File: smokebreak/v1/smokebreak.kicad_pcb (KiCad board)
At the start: 4 copper layers, 94 x 52 mm, 186 parts, among them J1 XT60 male, J2 XT30 male, J3 XT60 female, J4 XT30 female, J5 JST-XH 9, J6 SWD, J7 TFT1901 FPC, J8 USB-C, Q1 input FET, Q10 BC817, Q2 output FET, Q3 DMP10H400SE, Q4 BC817, Q5 BC817, Q6 AO3401A, Q7 AO3401A, Q8 2N7002, Q9 AO3400A, SW1 ON-OFF-(ON), SW2 Limit -, SW3 Limit +, U1 TPS48000, U10 SN74AHCT1G125, U11 USBLC6-2SC6, U2 INA181A2, U3 LMR36506R5, U4 TLV75533, U5 STM32G0B1RBT6, U6 DRV5032FA, U7 74LVC1G11, U8 LMV331, U9 SN74LVC1G74

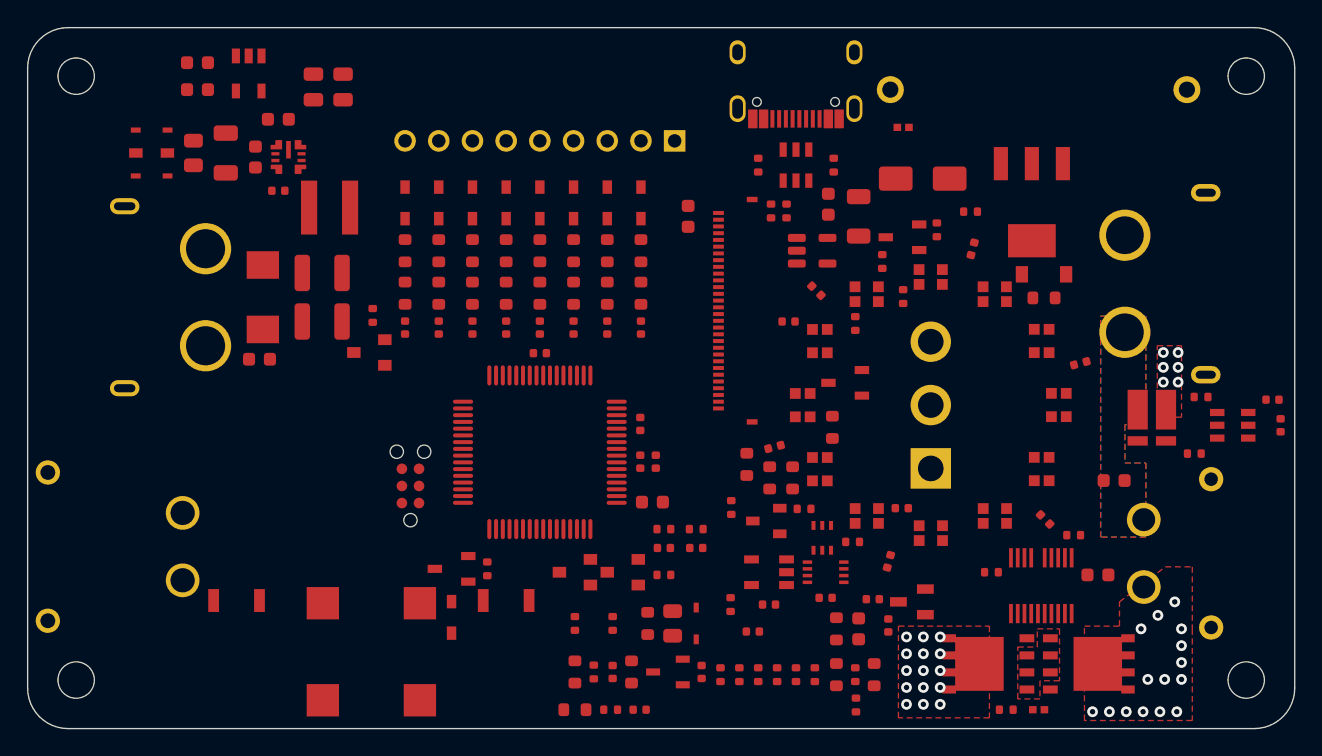
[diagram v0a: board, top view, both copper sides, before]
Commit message: smokebreak v1: simulation design values in the circuit (damper, snubber, Cdvdt, gate clamp, hard-short comparator, 2 x 15 Ohm pre-charge, DPAK pre-charge FET, 150 V probe PNPs), re-placed north-east, mesh 3D models
Co-Authored-By: Claude Opus 5.5 <noreply@anthropic.com>
Claude-Session: https://claude.ai/code/session_01SBnFJLvm1wBa1jZy4RXnma
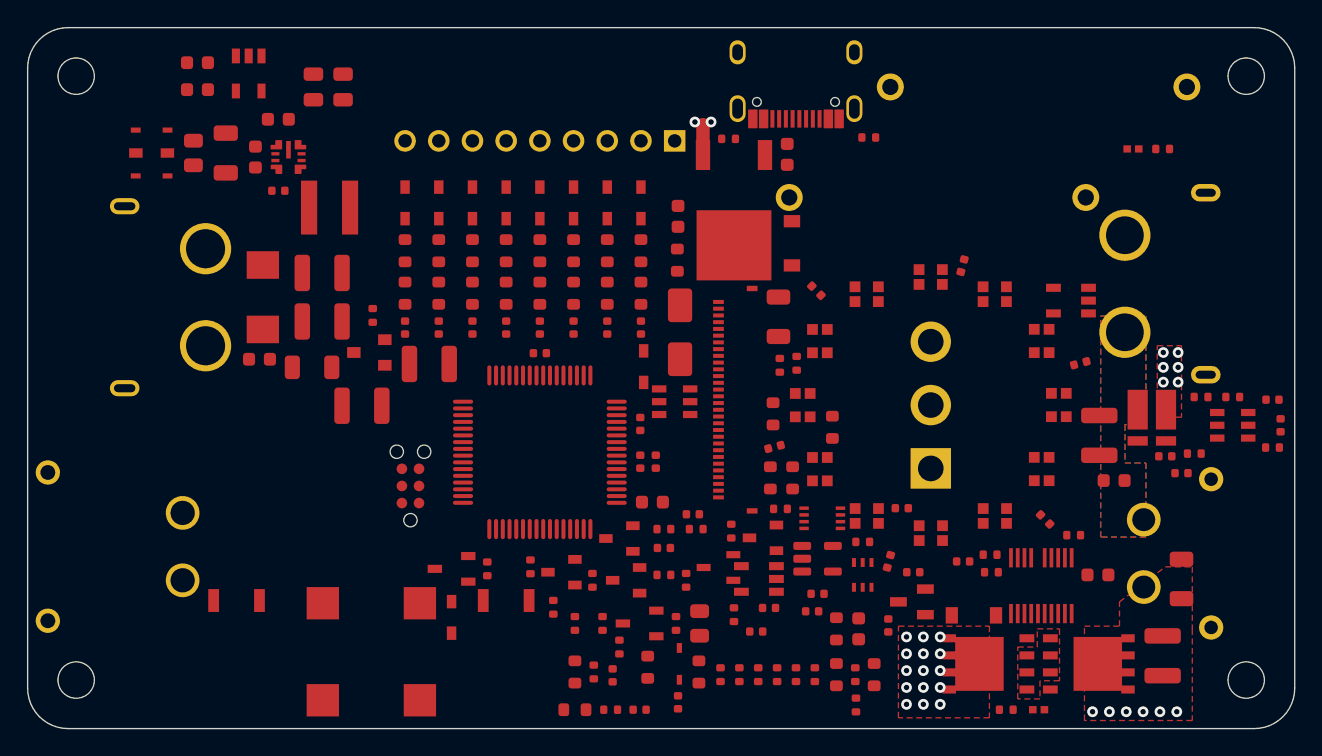
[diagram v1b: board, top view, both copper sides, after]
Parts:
- added C50: 4u7F 100V, C_1210_3225Metric, F.Cu at (129.8, 125.0)
- added C51: 4u7F 100V, C_1210_3225Metric, F.Cu at (124.8, 128.1)
- added C52: 4u7F 100V, C_1210_3225Metric, F.Cu at (184.2, 146.6)
- added C53: 4u7F 100V, C_1210_3225Metric, F.Cu at (179.5, 130.2)
- added C54: 22nF 50V, C_0402_1005Metric, F.Cu at (169.4, 139.6)
- added C55: 100nF 16V, C_0402_1005Metric, F.Cu at (184.4, 131.8)
- added C56: 100nF 16V, C_0402_1005Metric, F.Cu at (185.6, 133.1)
- added D18: 15 V, SOD-123_L2.7-W1.6-LS3.7-RD, F.Cu at (170.2, 143.6)
- added D19: 1N4148WS, SOD-323_L1.8-W1.3-LS2.5-RD, F.Cu at (145.7, 125.2)
- added R67: 0.33 Ohm, R_1206_3216Metric, F.Cu at (121.1, 125.2)
- added R68: 0.47 Ohm, R_1206_3216Metric, F.Cu at (185.6, 140.9)
- added R69: 1 k, R_0402_1005Metric, F.Cu at (171.4, 139.1)
- added R70: 39 k, R_0402_1005Metric, F.Cu at (189.4, 127.4)
- added R71: 1 k, R_0402_1005Metric, F.Cu at (192.3, 131.2)
- added R72: 4.7 k, R_0402_1005Metric, F.Cu at (137.3, 140.0)
- added R73: 820 Ohm, R_0402_1005Metric, F.Cu at (139.0, 143.0)
- added R_PRE2: 15 Ohm 5 W, RES-TH_BD7.5-L18.0-P22.00-D1.0, F.Cu at (167.5, 112.6)
- added U12: LMV331, SOT-23-5_L3.0-W1.7-P0.95-LS2.8-BR, F.Cu at (177.4, 120.2)
- Q3: value DMP10H400SE -> SUD50P10-43L; footprint SOT-223_L6.5-W3.5-P2.30-LS7.0-BR -> TO-252-3_L6.5-W5.8-P4.58-BR
- Q4: value BC817 -> MMBTA42; footprint SOT-23-3_L2.9-W1.6-P1.90-LS2.8-BR -> SOT-23-3_L2.9-W1.3-P1.90-LS2.4-BR
- Q6, Q7: value AO3401A -> MMBT5401; footprint SOT-23_L2.9-W1.3-P1.90-LS2.4-BR -> SOT-23-3_L2.9-W1.3-P1.90-LS2.4-BR
- R6: value 47 Ohm -> 100 k
- R9: value 15.4 k -> 40.2 k
- R_PRE: value 22 Ohm 5 W -> 15 Ohm 5 W
- moved R23 36.5 mm to (141.9, 141.0)
- moved R24 32.9 mm to (142.7, 144.2)
- moved Q4 32.7 mm to (144.4, 141.0)
- moved R21 27.8 mm to (148.8, 141.0)
- moved R19 27.3 mm to (148.2, 117.2), turned to 90 degrees
- moved R22 25.9 mm to (148.1, 144.2)
- moved Q5 23.5 mm to (145.4, 144.2)
- moved U10 22.9 mm to (158.6, 139.4)
- moved Q3 22.1 mm to (152.4, 112.8)
- moved D3 21.3 mm to (148.4, 122.6), turned to 90 degrees
- moved C42 20.3 mm to (158.6, 142.0)
- moved U11 19.7 mm to (148.0, 127.8), turned to 90 degrees
- moved D2 18.8 mm to (156.7, 116.0), turned to 90 degrees
- moved LED1 18.4 mm to (162.2, 136.2), turned to 180 degrees
- moved LED10 18.4 mm to (175.2, 132.8), turned to -90 degrees
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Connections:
- Q6 pad 1: PROBE_1K_N -> PROBE_BB1
- Q7 pad 1: PROBE_100_N -> PROBE_BB2
- R20 pad 2: PRE_PULL -> PRE_R
- R26 pad 1: PROBE_1K_N -> PROBE_BB1
- R27 pad 1: PROBE_100_N -> PROBE_BB2
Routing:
- net VIN: track 0.00 -> 2.20 mm, vias 15 -> 17
- net VOUT: vias 15 -> 6

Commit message: smokebreak v1: reverse-battery FET Q11 in the battery return (sims pass 22/22 with small damper and snubber), balance black wire through 10 Ohm, placement DRC clean
Co-Authored-By: Claude Opus 5.5 <noreply@anthropic.com>
Claude-Session: https://claude.ai/code/session_01SBnFJLvm1wBa1jZy4RXnma
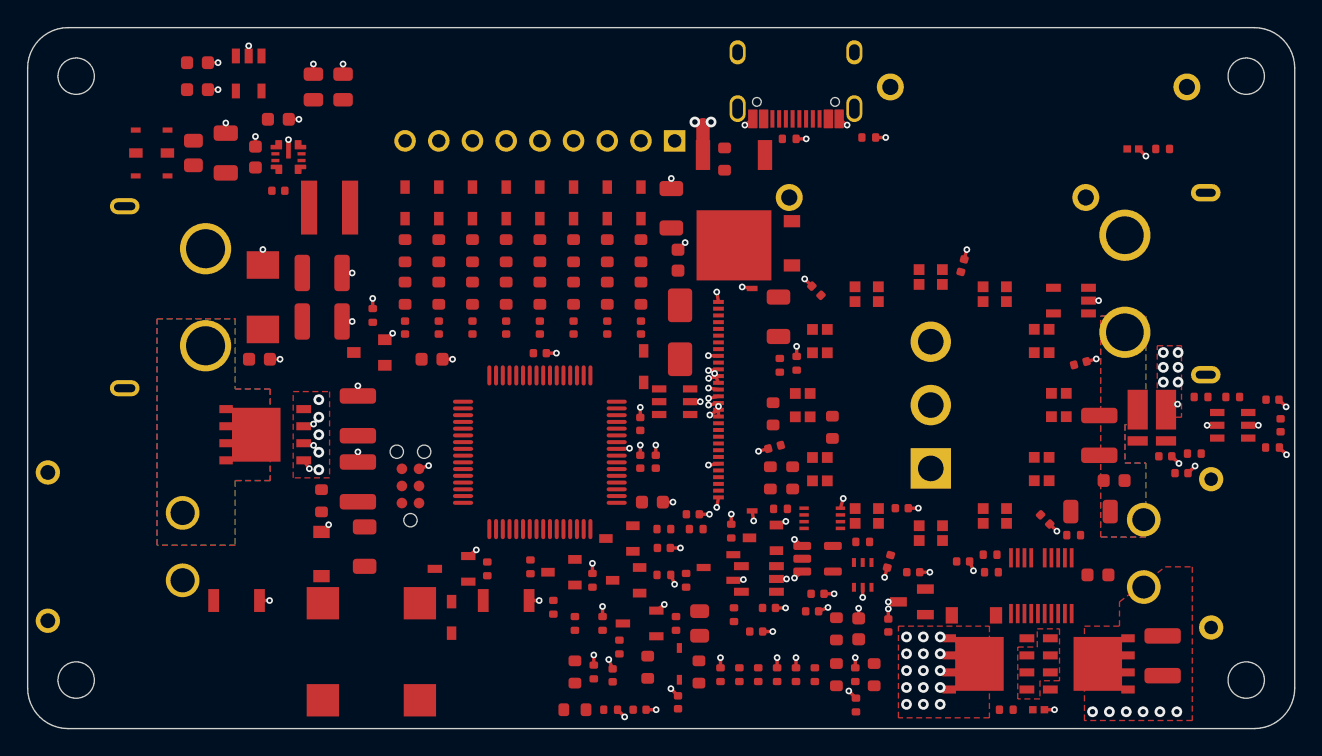
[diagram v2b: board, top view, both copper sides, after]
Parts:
- added D20: 12 V, SOD-123_L2.7-W1.6-LS3.7-RD, F.Cu at (121.8, 139.1)
- added Q11: BSC070N10LS5, PG-TDSON-8_L5.9-W5.1-P1.27-LS6.1-BL, F.Cu at (117.6, 130.2)
- added R74: 4.7 M, R_0603_1608Metric, F.Cu at (121.8, 135.1)
- added R75: 10 Ohm, R_1206_3216Metric, F.Cu at (147.8, 113.4)
- R70: value 39 k -> 49.9 k
- moved C49 30.4 mm to (130.0, 124.6), turned to 0 degrees
- moved R67 13.9 mm to (125.0, 138.5), turned to 90 degrees
- moved R68 8.40 mm to (178.8, 135.9), turned to 0 degrees
- moved R19 8.28 mm to (151.7, 109.8)
- moved C50 6.55 mm to (124.5, 128.8), turned to 90 degrees
- moved C51 5.66 mm to (124.5, 133.7), turned to 90 degrees
- moved R63 4.50 mm to (156.5, 108.2)
- moved C41 3.25 mm to (148.2, 117.2)
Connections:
- J1 pad 1: GND -> BATT_NEG
- J2 pad 1: GND -> BATT_NEG
- J5 pad 1: GND -> BAL1
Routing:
- net GND: track 0.00 -> 78.8 mm, vias 6 -> 115
- added copper zone on B.Cu, net BATT_NEG
- added copper zone on F.Cu, net BATT_NEG

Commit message: smokebreak v1: placed board with the TPS48000 move and ground fan-out
Co-Authored-By: Claude Opus 5.5 <noreply@anthropic.com>
Claude-Session: https://claude.ai/code/session_01SBnFJLvm1wBa1jZy4RXnma
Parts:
- moved C5 17.4 mm to (162.2, 142.5)
- moved U1 15.1 mm to (161.7, 148.1), turned to -90 degrees
- moved U12 10.9 mm to (179.4, 131.0)
- moved R32 10.8 mm to (139.1, 147.8)
- moved R5 9.55 mm to (168.2, 143.5)
- moved U9 9.39 mm to (150.4, 140.4)
- moved R4 6.75 mm to (156.1, 148.0)
- moved U7 6.50 mm to (168.4, 140.3)
- moved C53 6.50 mm to (179.5, 136.8)
- moved R7 6.03 mm to (176.6, 143.6)
- moved R6 5.85 mm to (165.7, 140.3)
- moved R68 5.75 mm to (178.8, 141.7)
- moved D5 4.81 mm to (147.0, 137.8)
- moved C12 4.70 mm to (169.9, 142.4)
- moved R69 4.67 mm to (169.8, 143.5)
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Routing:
- net GND: track 78.8 -> 78.5 mm, vias 115 -> 114

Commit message: smokebreak v1: 6-layer stack (F sig, In1 GND, In2/In3 sig, In4 VIN|VOUT power, B sig) - the 4-layer board could not route the control district
Co-Authored-By: Claude Opus 5.5 <noreply@anthropic.com>
Claude-Session: https://claude.ai/code/session_01SBnFJLvm1wBa1jZy4RXnma
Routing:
- added copper zone on In4.Cu, net VIN
- added copper zone on In4.Cu, net VOUT
- removed copper zone on In2.Cu, net VIN
- removed copper zone on In2.Cu, net VOUT
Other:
- copper layers 4 -> 6

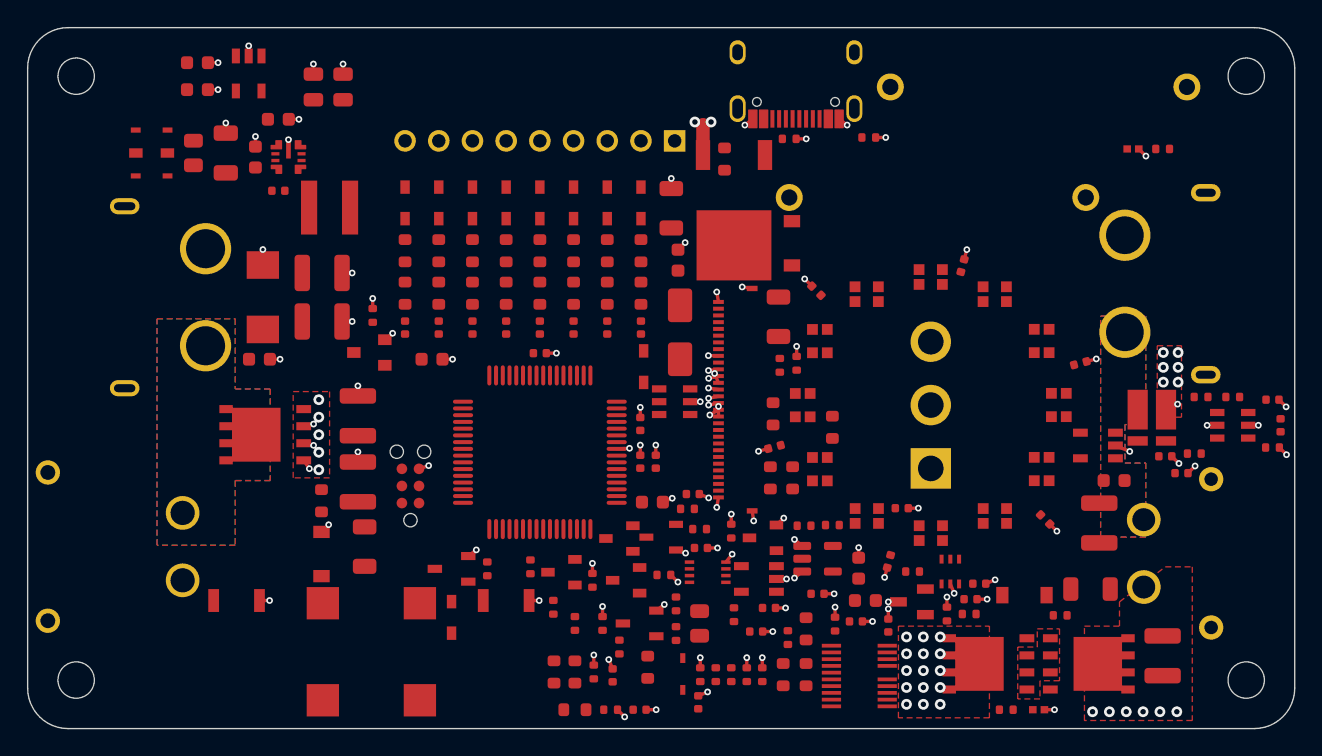
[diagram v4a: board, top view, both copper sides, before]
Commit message: smokebreak v1 (WIP): 6-layer board routed to 20 open connections, art on the bottom
Co-Authored-By: Claude Opus 5.5 <noreply@anthropic.com>
Claude-Session: https://claude.ai/code/session_01SBnFJLvm1wBa1jZy4RXnma
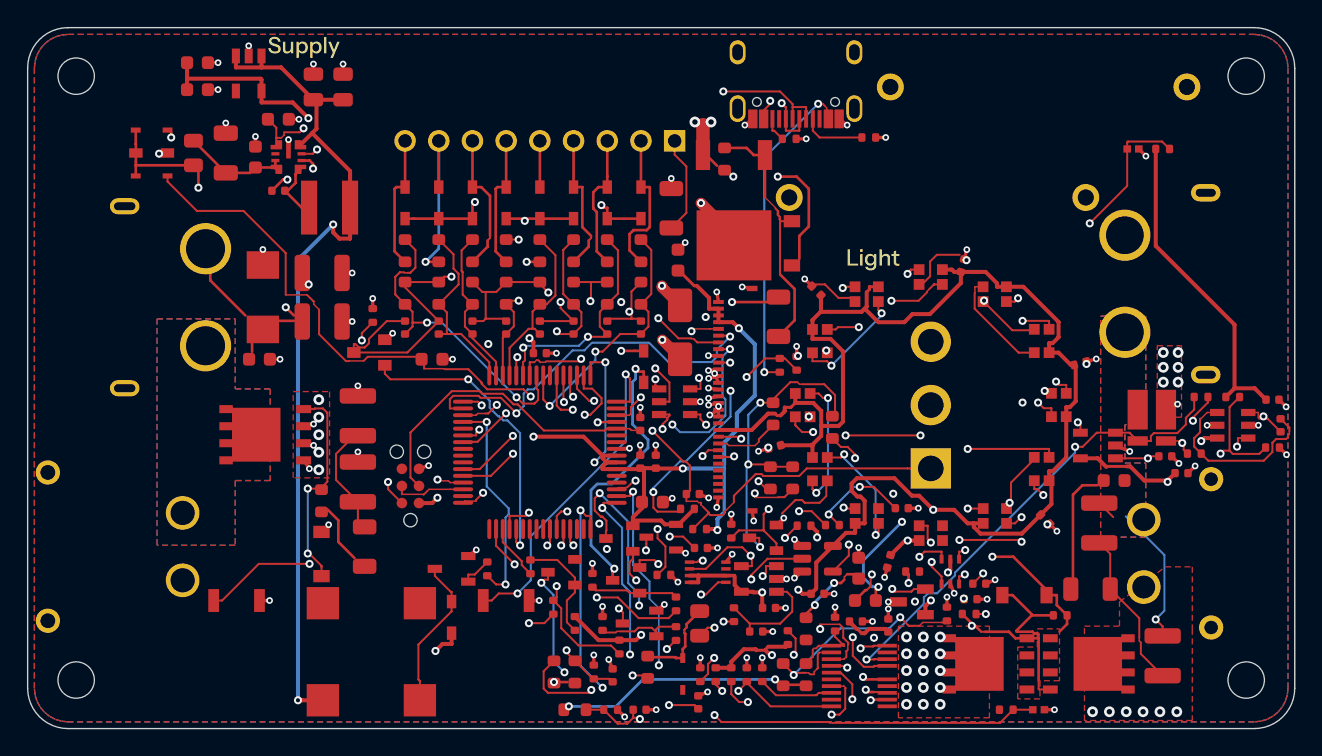
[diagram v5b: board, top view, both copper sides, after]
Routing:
- net +5V: track 0.00 -> 215.1 mm, vias 0 -> 6
- net +3V3: track 0.00 -> 207.1 mm, vias 0 -> 16
- net VBUS: track 0.00 -> 95.3 mm, vias 0 -> 5
- net VOUT: track 0.00 -> 61.7 mm, vias 6 -> 8
- net DIV_GND: track 0.00 -> 60.0 mm, vias 0 -> 5
- net NTC_FET: track 0.00 -> 57.6 mm, vias 0 -> 2
- net AUX: track 0.00 -> 56.2 mm, vias 0 -> 4
- net PEAK_OK: track 0.00 -> 54.8 mm, vias 0 -> 6
- net VIN: track 2.20 -> 53.1 mm, vias 17 -> 24
- net I_SENSE: track 0.00 -> 49.5 mm, vias 0 -> 3
- net GUARD_OPEN: track 0.00 -> 44.6 mm, vias 0 -> 4
- net TOG_ON: track 0.00 -> 44.2 mm, vias 0 -> 4
- net VOUT_LO: track 0.00 -> 43.4 mm, vias 0 -> 4
- net SNS_GND: track 0.00 -> 41.5 mm, vias 0 -> 3
- net TPS_FLT: track 0.00 -> 40.2 mm, vias 0 -> 4
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- added copper zone on B.Cu, net GND
- added copper zone on In2.Cu, net GND
- added copper zone on In3.Cu, net GND

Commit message: smokebreak v1: placed board for the current routing run
Co-Authored-By: Claude Opus 5.5 <noreply@anthropic.com>
Claude-Session: https://claude.ai/code/session_01SBnFJLvm1wBa1jZy4RXnma
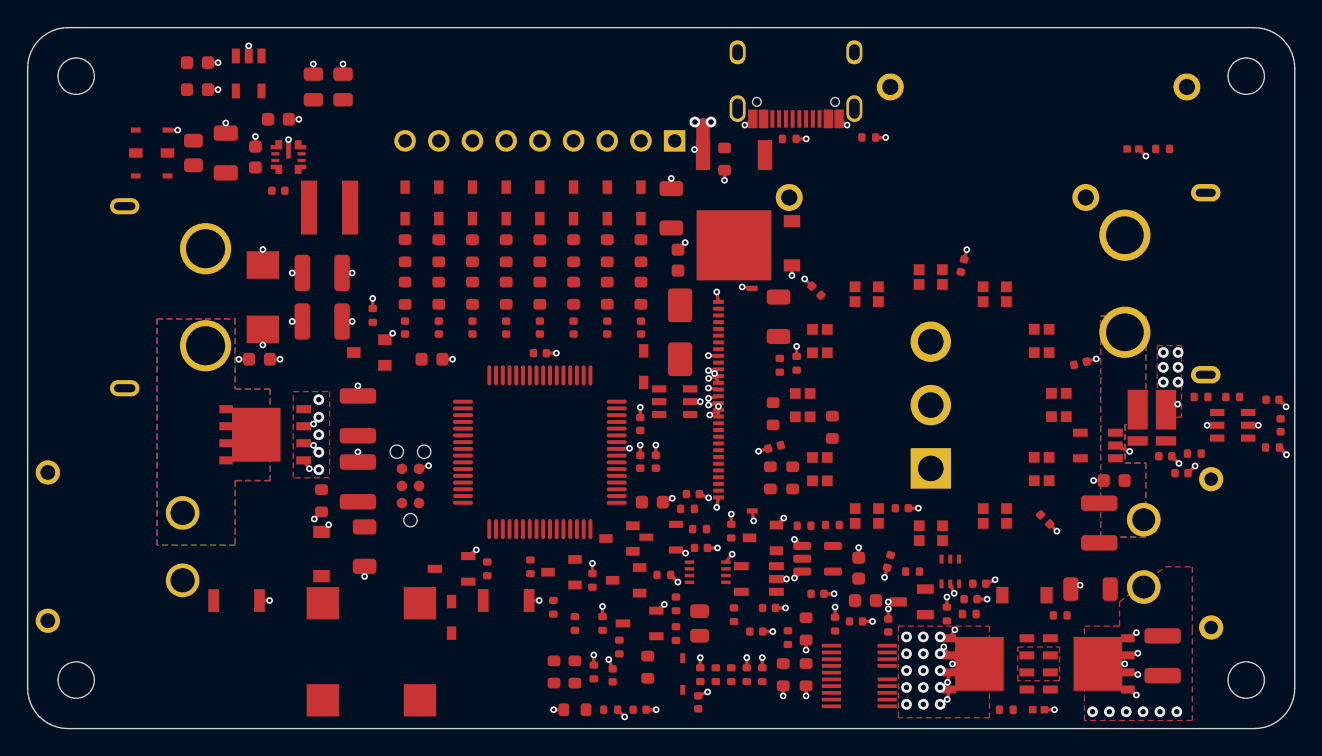
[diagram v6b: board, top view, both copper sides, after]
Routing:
- net +5V: track 215.1 -> 0.00 mm, vias 6 -> 0
- net +3V3: track 207.1 -> 0.00 mm, vias 16 -> 0
- net VBUS: track 95.3 -> 0.00 mm, vias 5 -> 0
- net DIV_GND: track 60.0 -> 0.00 mm, vias 5 -> 0
- net NTC_FET: track 57.6 -> 0.00 mm, vias 2 -> 0
- net AUX: track 56.2 -> 0.00 mm, vias 4 -> 0
- net VOUT: track 61.7 -> 6.50 mm, vias 8 -> 13
- net PEAK_OK: track 54.8 -> 0.00 mm, vias 6 -> 0
- net I_SENSE: track 49.5 -> 0.00 mm, vias 3 -> 0
- net GUARD_OPEN: track 44.6 -> 0.00 mm, vias 4 -> 0
- net TOG_ON: track 44.2 -> 0.00 mm, vias 4 -> 0
- net VOUT_LO: track 43.4 -> 0.00 mm, vias 4 -> 0
- net SNS_GND: track 41.5 -> 0.00 mm, vias 3 -> 0
- net TPS_FLT: track 40.2 -> 0.00 mm, vias 4 -> 0
- net MCU_EN: track 37.8 -> 0.00 mm, vias 3 -> 0
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- removed copper zone on B.Cu, net GND
- removed copper zone on In2.Cu, net GND
- removed copper zone on In3.Cu, net GND
